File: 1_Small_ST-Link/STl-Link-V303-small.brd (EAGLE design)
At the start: 25.4 x 18 mm, 31 parts

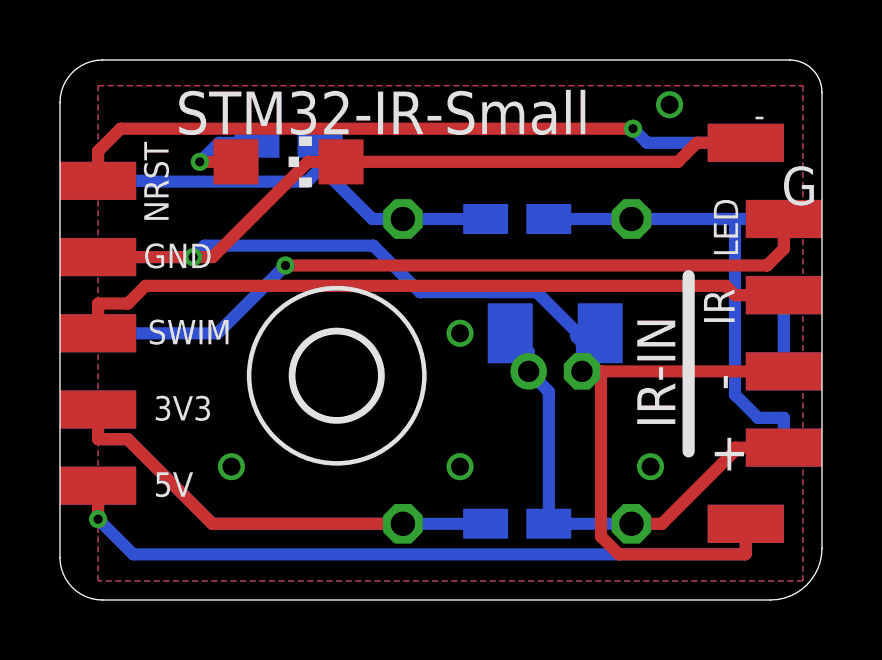
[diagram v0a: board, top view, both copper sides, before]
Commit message: LED removed
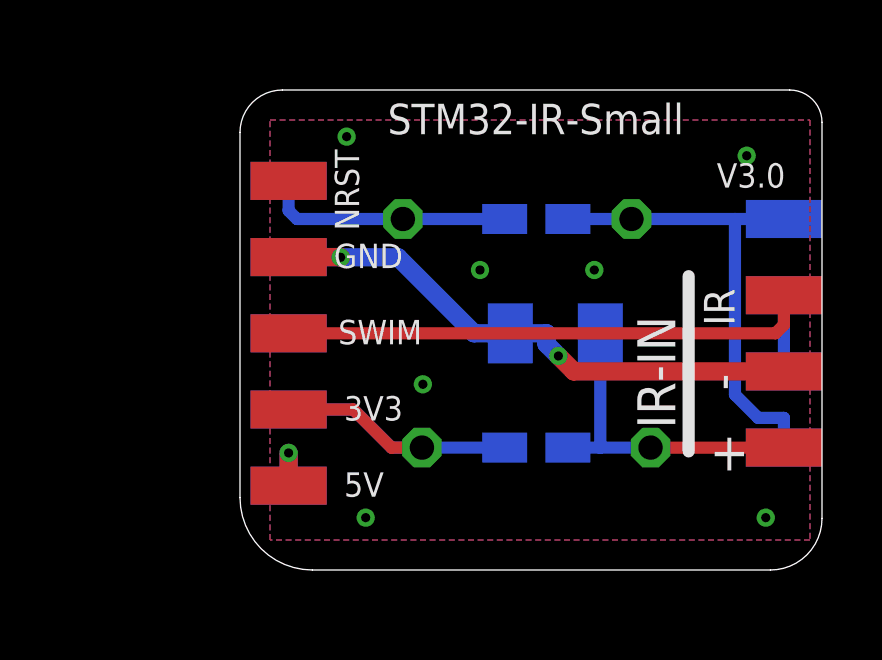
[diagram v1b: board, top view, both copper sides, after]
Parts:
- removed 5V, G, G3, IRS, LED: (no value), wirepad:SMD1,27-2,54
- removed C1: 4,7uF, rcl:E1,8-4
- removed H1: MOUNT-HOLE2.8, holes:2,8
- removed PWR: (no value), led:CHIPLED_1206
- removed R4: 220, rcl:R0805W
- moved 3V1 6.35 mm to (7.62, 6.35)
- moved 3V3 6.35 mm to (7.62, 6.35)
- moved 5V1 6.35 mm to (7.62, 3.81)
- moved 5V2 6.35 mm to (7.62, 3.81)
- moved DIO 6.35 mm to (7.62, 14.0)
- moved GND2 6.35 mm to (7.62, 11.4)
- moved GND3 6.35 mm to (7.62, 11.4)
- moved NRST 6.35 mm to (7.62, 14.0)
- moved SWCLK 6.35 mm to (7.62, 8.89)
- moved SWIM 6.35 mm to (7.62, 8.89)
- moved R2 2.62 mm to (15.9, 5.08)
- moved R3 2.62 mm to (15.9, 5.08)
- moved R7 0.63 mm to (15.9, 12.7)
- turned C2 to 0 degrees
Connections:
- removed net NRST-IR-SEND: IRS.1, NRST.1
- removed net OK: PWR.A, R4.2
- new net N$1: NRST.1
- net 5V: no longer 5V.1
- net CLK-TOGGLE-LED: no longer LED.1
- net DIO-EINSCH: no longer R4.1
- net GND: no longer C1.-, G.1, G3.1, PWR.C
- net IR+: no longer C1.+
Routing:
- net GND: track 61.0 -> 20.0 mm, vias 6 -> 9
- net CLK-TOGGLE-LED: track 25.0 -> 0.00 mm, vias 1 -> 0
- net 5V: track 25.3 -> 2.18 mm
- net NRST-IR-SEND: track 23.1 -> 0.00 mm, vias 1 -> 0
- net 3V3: track 27.4 -> 12.7 mm
- net SWIM-IR-IN: track 24.2 -> 17.6 mm
- net DIO-EINSCH: track 14.7 -> 8.31 mm
- net IR+: track 15.8 -> 11.0 mm
- net OK: track 3.38 -> 0.00 mm, vias 1 -> 0
- net PWR+: track 16.6 -> 16.0 mm
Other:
- board size 25.4 x 18 mm -> 19.4 x 16 mm
- board text added: "V3.0"
- board text removed: "220R_LED"
- board text removed: "IRSen"
- board text removed: "LED"
- board text removed: "V3.0 www.neuby.de"
